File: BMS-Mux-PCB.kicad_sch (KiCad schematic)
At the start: 39 parts, among them J1 Conn_02x10_Counter_Clockwise, J18 Conn_01x02, J19 Conn_01x02, J2 Conn_02x08_Counter_Clockwise, J3 Conn_02x10_Counter_Clockwise, J4 Conn_02x08_Counter_Clockwise, Q1 DMP10H4D2S, Q2 BSS123, Q3 BSS123, U1 74CBTLV3257, U2 74CBTLV3257, U3 6-36Vin, 3.3Vout, 1Aout, U4 TMR_1-4812

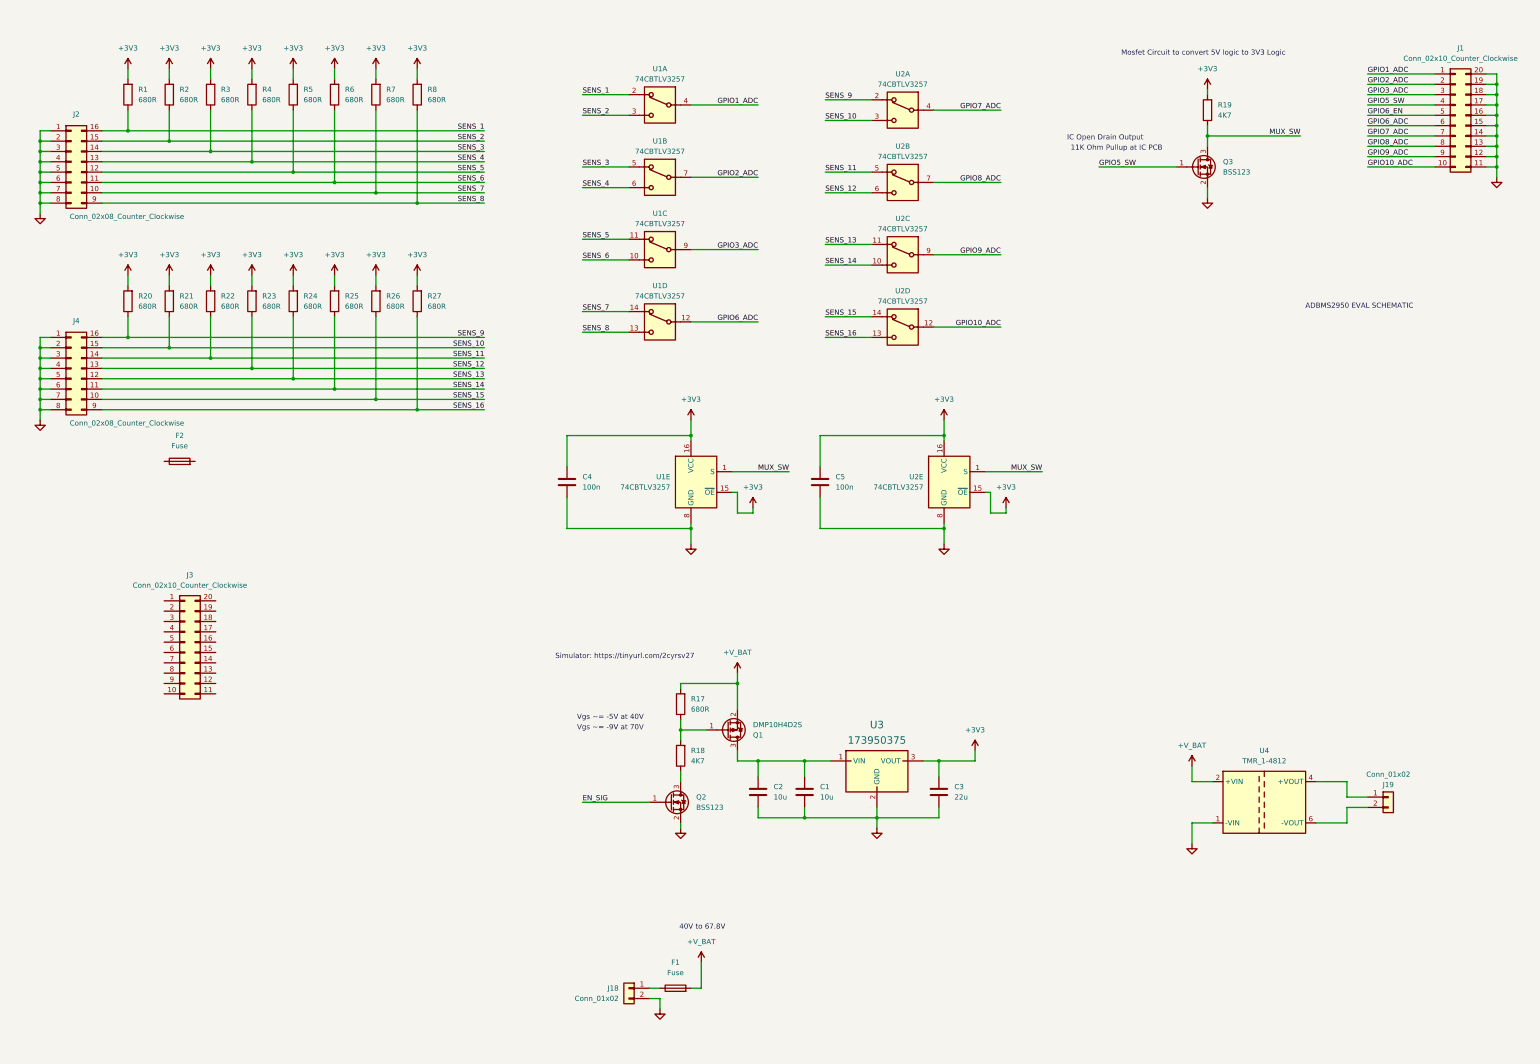
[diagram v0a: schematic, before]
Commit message: Finished Schematic -> fuse and connector footprint needs changing
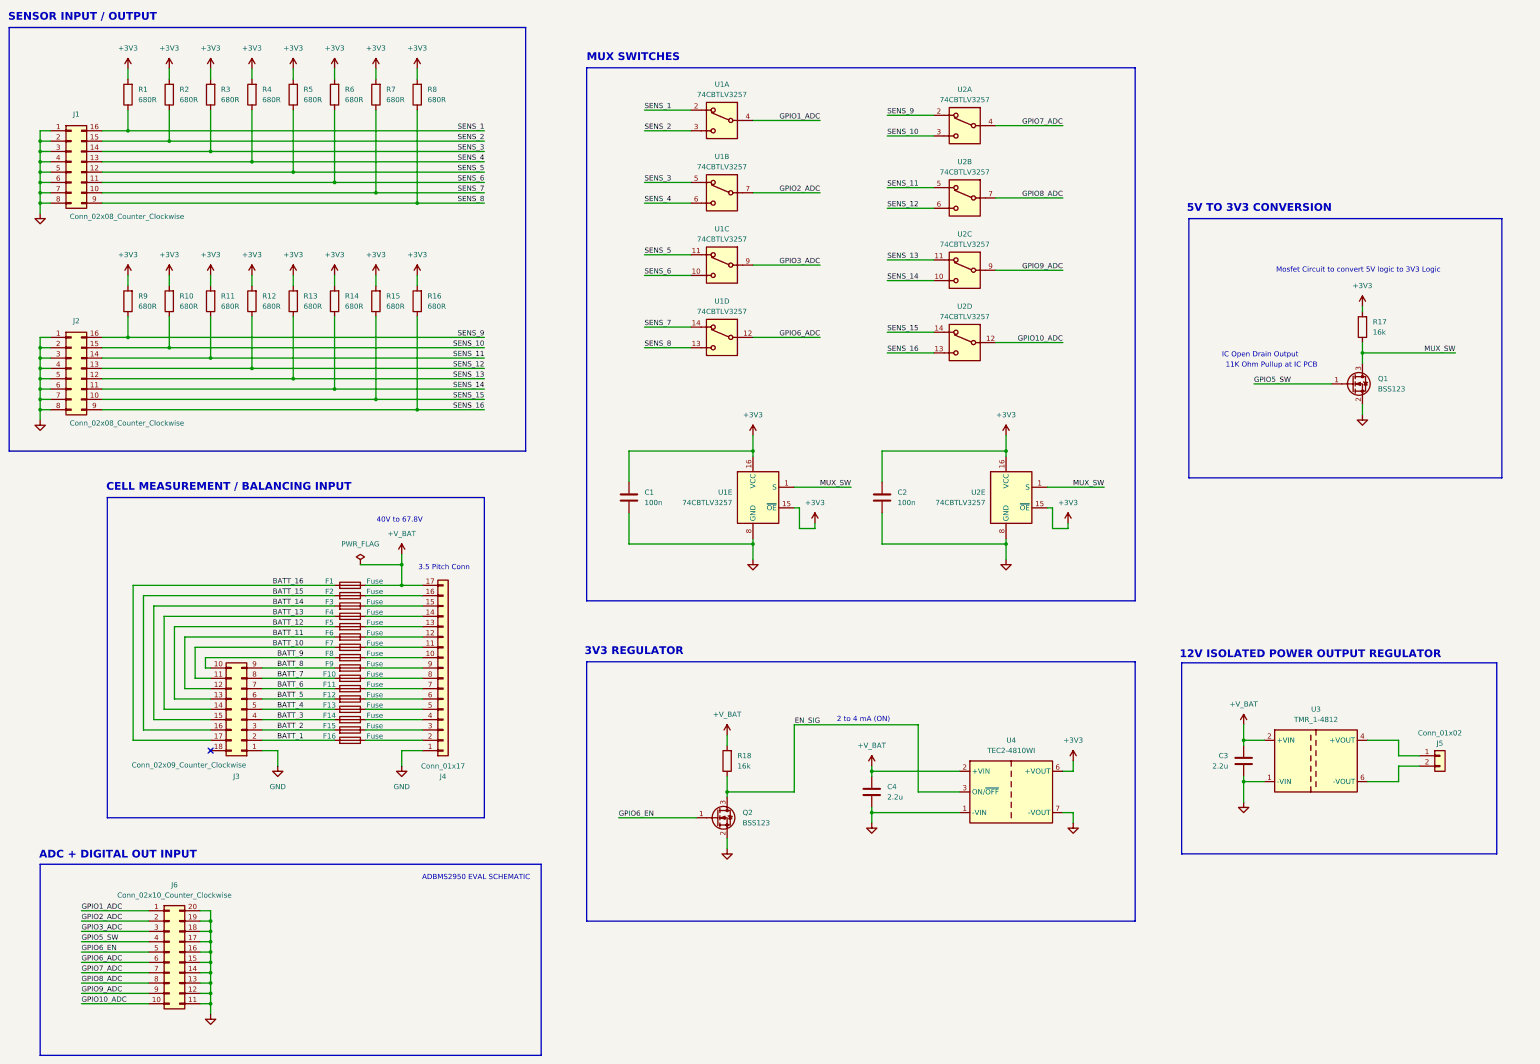
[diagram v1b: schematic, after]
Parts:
- removed C2: 10u, symbol Device:C
- removed J18: Conn_01x02, symbol Connector_Generic:Conn_01x02
- removed J3: Conn_02x10_Counter_Clockwise, symbol Connector_Generic:Conn_02x10_Counter_Clockwise
- removed Q1: DMP10H4D2S, Package_TO_SOT_SMD:SOT-23, symbol BMS-Mux-library:DMP10H4D2S
- removed R17: 680R, symbol Device:R
- removed U3: 6-36Vin, 3.3Vout, 1Aout, MagIC-FDSM (rev22e):WPME-FDSM_SIP-3_L11.6W8H10.4, symbol BMS-Mux-library:173950375
- added F10, F11, F12, F13, F14, F15, F16, F3, F4, F5, F6, F7, F8, F9: Fuse, Fuse:Fuse_2512_6332Metric_Pad1.52x3.35mm_HandSolder, symbol Device:Fuse
- added J3: Conn_02x09_Counter_Clockwise, Connector_Molex:Molex_Micro-Fit_3.0_43045-1800_2x09_P3.00mm_Horizontal, symbol Connector_Generic:Conn_02x09_Counter_Clockwise
- added J4: Conn_01x17, Connector_TE-Connectivity:TE_1-826576-7_1x17_P3.96mm_Vertical, symbol Connector_Generic:Conn_01x17
- added U4: TEC2-4810WI, Converter_DCDC:Converter_DCDC_TRACO_TMR-xxxx_THT, symbol Converter_DCDC:TEC2-4810WI
- C1: renamed from C4; footprint (none) -> Capacitor_SMD:C_0603_1608Metric_Pad1.08x0.95mm_HandSolder
- C2: renamed from C5; footprint (none) -> Capacitor_SMD:C_0603_1608Metric_Pad1.08x0.95mm_HandSolder
- C3: value 22u -> 2.2u; footprint (none) -> Capacitor_SMD:C_1206_3216Metric_Pad1.33x1.80mm_HandSolder
- C4: renamed from C1; value 10u -> 2.2u; footprint (none) -> Capacitor_SMD:C_1206_3216Metric_Pad1.33x1.80mm_HandSolder
- F1, F2: footprint (none) -> Fuse:Fuse_2512_6332Metric_Pad1.52x3.35mm_HandSolder
- J1: renamed from J2; footprint (none) -> Connector_Molex:Molex_Micro-Fit_3.0_43045-1600_2x08_P3.00mm_Horizontal
- J2: renamed from J4; footprint (none) -> Connector_Molex:Molex_Micro-Fit_3.0_43045-1600_2x08_P3.00mm_Horizontal
- J5: renamed from J19; footprint (none) -> Connector_Molex:Molex_Micro-Fit_3.0_43650-0200_1x02_P3.00mm_Horizontal
- J6: renamed from J1; footprint (none) -> Connector_Molex:Molex_Micro-Fit_3.0_43045-2000_2x10_P3.00mm_Horizontal
- R1, R2, R3, R4, R5, R6, R7, R8: footprint (none) -> Resistor_SMD:R_0805_2012Metric
- R10: renamed from R21; footprint (none) -> Resistor_SMD:R_0805_2012Metric
- R11: renamed from R22; footprint (none) -> Resistor_SMD:R_0805_2012Metric
- R12: renamed from R23; footprint (none) -> Resistor_SMD:R_0805_2012Metric
- R13: renamed from R24; footprint (none) -> Resistor_SMD:R_0805_2012Metric
- R14: renamed from R25; footprint (none) -> Resistor_SMD:R_0805_2012Metric
- R15: renamed from R26; footprint (none) -> Resistor_SMD:R_0805_2012Metric
- R16: renamed from R27; footprint (none) -> Resistor_SMD:R_0805_2012Metric
- R17: renamed from R19; value 4K7 -> 16k; footprint (none) -> Resistor_SMD:R_0805_2012Metric
- R18: value 4K7 -> 16k; footprint (none) -> Resistor_SMD:R_0805_2012Metric
- R9: renamed from R20; footprint (none) -> Resistor_SMD:R_0805_2012Metric
- U1, U2: footprint (none) -> Package_SO:SOIC-16_3.9x9.9mm_P1.27mm
- renumbered Q3 to Q1, U4 to U3
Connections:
- net +3V3: now also U4.6 (+VOUT); no longer C3.1
- net +V_BAT: now also C3.1, C4.1, F1.1, R18.2, J4.17 (Pin_17), U4.2 (+VIN); no longer F1.2
- net EN_SIG: now also Q2.3 (D), R18.1, U4.3 (ON/~{OFF}); no longer Q2.1 (G)
- net GND: now also J3.1 (Pin_1), J4.1 (Pin_1), U4.1 (-VIN), U4.7 (-VOUT)
- net GPIO6_EN: now also Q2.1 (G)
- net at F2.1: now also J4.16 (Pin_16)
- net BATT_15: now reaches F2.2
- net BATT_15: now also J3.16 (Pin_16)
- new net: F13.1, J4.5 (Pin_5)
- new net: F9.1, J4.9 (Pin_9)
- new net: F11.1, J4.7 (Pin_7)
- new net: F6.1, J4.12 (Pin_12)
- new net: F16.1, J4.2 (Pin_2)
- new net: F8.1, J4.10 (Pin_10)
- new net: F7.1, J4.11 (Pin_11)
- new net: F5.1, J4.13 (Pin_13)
- new net: F10.1, J4.8 (Pin_8)
- new net: F14.1, J4.4 (Pin_4)
- new net: F3.1, J4.15 (Pin_15)
- new net: F4.1, J4.14 (Pin_14)
- new net: F15.1, J4.3 (Pin_3)
- new net: F12.1, J4.6 (Pin_6)
- new net BATT_1: F16.2, J3.2 (Pin_2)
- new net BATT_10: F7.2, J3.11 (Pin_11)
- new net BATT_11: F6.2, J3.12 (Pin_12)
- new net BATT_12: F5.2, J3.13 (Pin_13)
- new net BATT_13: F4.2, J3.14 (Pin_14)
- new net BATT_14: F3.2, J3.15 (Pin_15)
- new net BATT_16: F1.2, J3.17 (Pin_17)
- new net BATT_2: F15.2, J3.3 (Pin_3)
- new net BATT_3: F14.2, J3.4 (Pin_4)
- new net BATT_4: F13.2, J3.5 (Pin_5)
- new net BATT_5: F12.2, J3.6 (Pin_6)
- new net BATT_6: F11.2, J3.7 (Pin_7)
- new net BATT_7: F10.2, J3.8 (Pin_8)
- new net BATT_8: F9.2, J3.9 (Pin_9)
- new net BATT_9: F8.2, J3.10 (Pin_10)
- no-connect marks 0 -> 1
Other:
- note added: "12V ISOLATED POWER OUTPUT REGULATOR"
- note added: "2 to 4 mA (ON)"
- note added: "3.5 Pitch Conn"
- note added: "3V3 REGULATOR"
- note added: "5V TO 3V3 CONVERSION"
- note added: "ADC + DIGITAL OUT INPUT"
- note added: "CELL MEASUREMENT / BALANCING INPUT"
- note added: "MUX SWITCHES"
- note added: "SENSOR INPUT / OUTPUT"
- note removed: "Simulator: https://tinyurl.com/2cyrsv27"
- note removed: "Vgs ~= -5V at 40V"
- note removed: "Vgs ~= -9V at 70V"
- moved on the sheet: C1, C2, C4, F2, J5, J6, Q1, R17, U1A, U1B, U1C, U1D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

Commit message: progress
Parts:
- removed J4: Conn_01x17, Connector_TE-Connectivity:TE_1-826576-7_1x17_P3.96mm_Vertical, symbol Connector_Generic:Conn_01x17
- added H1, H2, H3, H4: MountingHole_Pad, BMS-Mux-footprints:Mounting_Hole, symbol Mechanical:MountingHole_Pad
- added J4: Conn_01x18, Connector_Wago:Wago_734-148_1x18_P3.50mm_Vertical, symbol Connector_Generic:Conn_01x18
- F1, F10, F11, F12, F13, F14, F15, F16, F2, F3, F4, F5, F6, F7, F8, F9: footprint Fuse:Fuse_2512_6332Metric_Pad1.52x3.35mm_HandSolder -> Fuse:Fuse_1206_3216Metric_Pad1.42x1.75mm_HandSolder
- J6: footprint Connector_Molex:Molex_Micro-Fit_3.0_43045-2000_2x10_P3.00mm_Horizontal -> Connector_PinHeader_2.54mm:PinHeader_2x10_P2.54mm_Vertical
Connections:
- net +3V3: no longer U1.15 (~{OE}), U2.15 (~{OE})
- net +V_BAT: now also J4.17 (Pin_17)
- net GND: now also U1.15 (~{OE}), U2.15 (~{OE}), J4.1 (Pin_1)
- net at F13.1: now also J4.5 (Pin_5)
- net at F9.1: now also J4.9 (Pin_9)
- net at F11.1: now also J4.7 (Pin_7)
- net at F6.1: now also J4.12 (Pin_12)
- net at F16.1: now also J4.2 (Pin_2)
- net at F8.1: now also J4.10 (Pin_10)
- net at F7.1: now also J4.11 (Pin_11)
- net at F2.1: now also J4.16 (Pin_16)
- net at F5.1: now also J4.13 (Pin_13)
- net at F10.1: now also J4.8 (Pin_8)
- net at F14.1: now also J4.4 (Pin_4)
- net at F3.1: now also J4.15 (Pin_15)
- net at F4.1: now also J4.14 (Pin_14)
- net at F15.1: now also J4.3 (Pin_3)
- net at F12.1: now also J4.6 (Pin_6)
- no-connect marks 1 -> 6
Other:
- note added: "2 to 4 mA (OFF)"
- note added: "SENSOR INPUT"
- note added: "https://uk.rs-online.com/web/p/non-resettable-fuses/5413552?gb=s"
- note removed: "2 to 4 mA (ON)"
- note removed: "SENSOR INPUT / OUTPUT"
